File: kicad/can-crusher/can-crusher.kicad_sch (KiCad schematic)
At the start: 1 part

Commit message: Schematic Work in progress
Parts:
- added J?: Stepper Left, symbol Connector:Conn_01x04_Male
- added J?: Stepper Right, symbol Connector:Conn_01x04_Male
- added R?: 1000, symbol Device:R
- added SW?: Reboot, symbol Switch:SW_Push
- added U? (x2): BTT_TMC2209, symbol btt_tmc2209:BTT_TMC2209
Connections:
- net GND: now reaches U?.13 (GND)
- net GND: now also U?.18 (GND), U?.23 (GND), U?.28 (GND), U?.3 (GND), U?.33 (AGND), U?.38 (GND), U?.8 (GND), SW?.2, U?.15 (GND), U?.15 (GND), U?.5 (PDN), U?.5 (PDN), U?.6 (CLK), U?.6 (CLK), U?.9 (GND), U?.9 (GND)
- net at U?.14 (GPIO10): now also U?.1 (EN)
- net at U?.15 (GPIO11): now also U?.7 (STEP)
- net at U?.16 (GPIO12): now also U?.8 (DIR)
- net at U?.17 (GPIO13): now also U?.17 (DIAG)
- net at U?.19 (GPIO14): now also U?.2 (MS1)
- net at U?.20 (GPIO15): now also U?.3 (MS2)
- net at U?.21 (GPIO16): now also U?.3 (MS2)
- net at U?.22 (GPIO17): now also U?.2 (MS1)
- net at U?.24 (GPIO18): now also U?.17 (DIAG)
- net at U?.25 (GPIO19): now also U?.8 (DIR)
- net at U?.26 (GPIO20): now also U?.7 (STEP)
- net at U?.27 (GPIO21): now also U?.1 (EN)
- net at U?.30 (RUN): now also SW?.1
- net +3.3V: now reaches U?.36 (3V3)
- net +3.3V: now also U?.10 (VDD), U?.10 (VDD)
- net at U?.6 (GPIO4): now also R?.2
- net at U?.7 (GPIO5): now also R?.1, U?.4 (PDN), U?.4 (PDN)
- new net: J?.1 (Pin_1), U?.14 (A1) (x2)
- new net: J?.2 (Pin_2), U?.13 (A2) (x2)
- new net: J?.3 (Pin_3), U?.12 (B1) (x2)
- new net: J?.4 (Pin_4), U?.11 (B2) (x2)
- new net +12V: U?.16 (VM), U?.16 (VM)

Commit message: Schematic work-in-progress checkpoint
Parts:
- added J2: Control UART, symbol Connector:Conn_01x06_Female
- added J3: Ext power, symbol Connector:Conn_01x02_Male
- gave numbers to parts that had none: 7
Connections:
- net GND: now also J2.6 (Pin_6), J3.2 (Pin_2)
- net STEP_TXRX: now reaches U1.4 (PDN), U2.7 (GPIO5), U3.4 (PDN)
- net STEP_TXRX: now also R1.2; no longer R1.1
- net at U2.1 (GPIO0): now also J2.2 (Pin_2)
- net at U2.2 (GPIO1): now also J2.3 (Pin_3)
- net VCC: now reaches U2.39 (VSYS)
- net VCC: now also J3.1 (Pin_1)
- net at U2.6 (GPIO4): now also R1.1; no longer R1.2
- no-connect marks 0 -> 21
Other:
- note added: "ERC Flags"
- note added: "EXT POWER"
- note added: "External power when USB is disconnected. 1.8-5.5 volts regulated by onboard Pico buck/boost."
- note added: "For future interface so we don't need to recompile code to exercise and test motors."
- note added: "STEPPER TX/UX"
- note added: "Single wire RS483 style protocol is used to set advanced controls on TMC2209"
- note added: "UART Control Port"
- moved on the sheet: J1, J4, R1, SW1, U1, U2, U3

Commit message: Initial first pass of PCB design
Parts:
- added D1: LED_RGBK, symbol Device:LED_RGBK
- added J5: Barrel_Jack, symbol Connector:Barrel_Jack
- added J6: Expansion Port, symbol Connector:Conn_01x08_Female
- added Q1: IRF4905, Package_TO_SOT_THT:TO-220-3_Vertical, symbol Transistor_FET:IRF4905
- added R2, R3, R4: R, symbol Device:R
- added R5: 0, symbol Device:R
- added R6: 50k, symbol Device:R
- added SW2: User Interaction, symbol Switch:SW_Push
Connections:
- net +12V: now also J5.1, Q1.3 (S), R5.1, R6.2; no longer U1.16 (VM), U3.16 (VM)
- net +3.3V: now also J6.7 (Pin_7)
- net GND: now also D1.4 (K), J5.2, J6.8 (Pin_8), SW2.1
- net at U2.10 (GPIO7): now also R3.1
- net at U2.11 (GPIO8): now also R4.1
- net at U2.12 (GPIO9): now also SW2.2
- net at U2.29 (GPIO22): now also Q1.1 (G), R6.1
- net at U2.31 (GPIO26_ADC0): now also J6.3 (Pin_3)
- net at U2.32 (GPIO27_ADC1): now also J6.4 (Pin_4)
- net at U2.34 (GPIO28_ADC2): now also J6.5 (Pin_5)
- net at U2.35 (ADC_VREF): now also J6.6 (Pin_6)
- net at U2.4 (GPIO2): now also J6.1 (Pin_1)
- net at U2.5 (GPIO3): now also J6.2 (Pin_2)
- net at U2.9 (GPIO6): now also R2.1
- new net: D1.2 (GA), R3.2
- new net: D1.1 (RA), R2.2
- new net: D1.3 (BA), R4.2
- new net 12V_ON: Q1.2 (D), R5.2, U1.16 (VM), U3.16 (VM)
- no-connect marks 21 -> 10
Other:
- note added: "EXPANSION PORT"
- note added: "EXT MCU POWER"
- note added: "EXT STEPPER POWER"
- note added: "For testing give some LED color feedback and a button the user can press, so we don't always need to watch the debug logs to understand what's going on."
- note added: "LEFT Z-AXIS STEPPER CONTROL"
- note added: "Lite User Interface"
- note added: "RIGHT Z-AXIS STEPPER CONTROL"
- note added: "SOFT REBOOT SWITCH"
- note added: "Stepper motors can take anywhere between 9-24 volts. We'll just use a barrel jack and use a pre-built power supply. A P-Channel Mosfet with a Pull-Up makes us explicitly let power flow to the stepper drivers via GPIO22. Include an NC 0-ohm resistor to bypass the switch in case the design is totally wrong."
- note added: "Throw all the unused pins to a header so we can add in a few more components without having to respin the board."
- note removed: "EXT POWER"
- moved on the sheet: J1, J4, R1, SW1, U1, U3

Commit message: Added title comments, etc, to title block
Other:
- company: (none) -> https://github.com/grant-olson/can-crusher
- title: (none) -> Can Crusher Dev Board
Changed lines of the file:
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@@
 (kicad_sch (version 20211123) (generator eeschema)
   (paper "A4")
+  (title_block
+    (title "Can Crusher Dev Board")
+    (date "2022-10-10")
+    (rev "1")
+    (company "https://github.com/grant-olson/can-crusher")
+    (comment 1 "Control board for the most technilogically advanced aluminum can crusher IN THE WORLD.")
+  )
   (junction (at 207.01 46.99) (diameter 0) (color 0 0 0 0)
   )

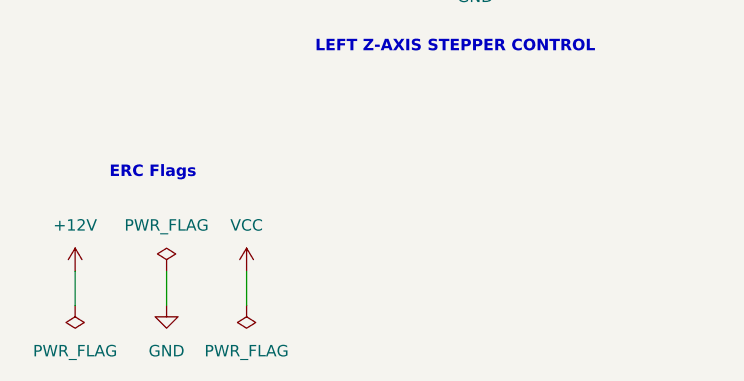
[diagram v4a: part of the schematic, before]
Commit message: Fixes for ERC checks
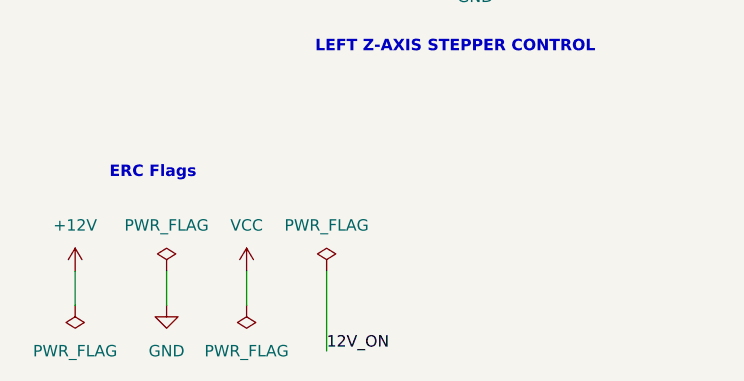
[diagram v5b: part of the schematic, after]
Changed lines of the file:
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@@
+    (stroke (width 0) (type default) (color 0 0 0 0))
+  )
+  (wire (pts (xy 49.53 184.15) (xy 49.53 193.04))
     (stroke (width 0) (type default) (color 0 0 0 0))
   )
@@
   (text "Single wire RS483 style \nprotocol is used to set \nadvanced controls on\nTMC2209\n"
     (at 88.9 26.67 0)
+    (effects (font (size 1.27 1.27)) (justify left bottom))
+  )
+  (label "12V_ON" (at 49.53 193.04 0)
     (effects (font (size 1.27 1.27)) (justify left bottom))
   )
@@
     (pin "1")
   )
-  (symbol (lib_name "BTT_TMC2209_1") (lib_id "btt_tmc2209:BTT_TMC2209") (at 237.49 118.11 0) (unit 1)
+  (symbol (lib_id "btt_tmc2209:BTT_TMC2209") (at 237.49 118.11 0) (unit 1)
     (in_bom yes) (on_board yes)
     (property "Reference" "U3" (id 0) (at 239.395 142.24 0))
@@
     (pin "1")
   )
+  (symbol (lib_id "power:PWR_FLAG") (at 49.53 184.15 0) (unit 1)
+    (in_bom yes) (on_board yes) (fields_autoplaced)
+    (property "Reference" "#FLG0102" (id 0) (at 49.53 182.245 0)
+      (effects (font (size 1.27 1.27)) hide)
+    )
+    (property "Value" "PWR_FLAG" (id 1) (at 49.53 179.07 0))
+    (property "Footprint" "" (id 2) (at 49.53 184.15 0)
+      (effects (font (size 1.27 1.27)) hide)
+    )
+    (property "Datasheet" "~" (id 3) (at 49.53 184.15 0)
+      (effects (font (size 1.27 1.27)) hide)
+    )
+    (pin "1")
+  )
   (symbol (lib_id "power:GND") (at 66.04 148.59 0) (unit 1)
     (in_bom yes) (on_board yes) (fields_autoplaced)
@@
       (reference "#FLG0101") (unit 1) (value "PWR_FLAG") (footprint "")
     )
+    (path "/8f9714ab-2f22-4d0c-918a-f2e6cc76e015"
+      (reference "#FLG0102") (unit 1) (value "PWR_FLAG") (footprint "")
+    )
     (path "/8a4f5206-01a9-48d1-8d82-8554a491299f"

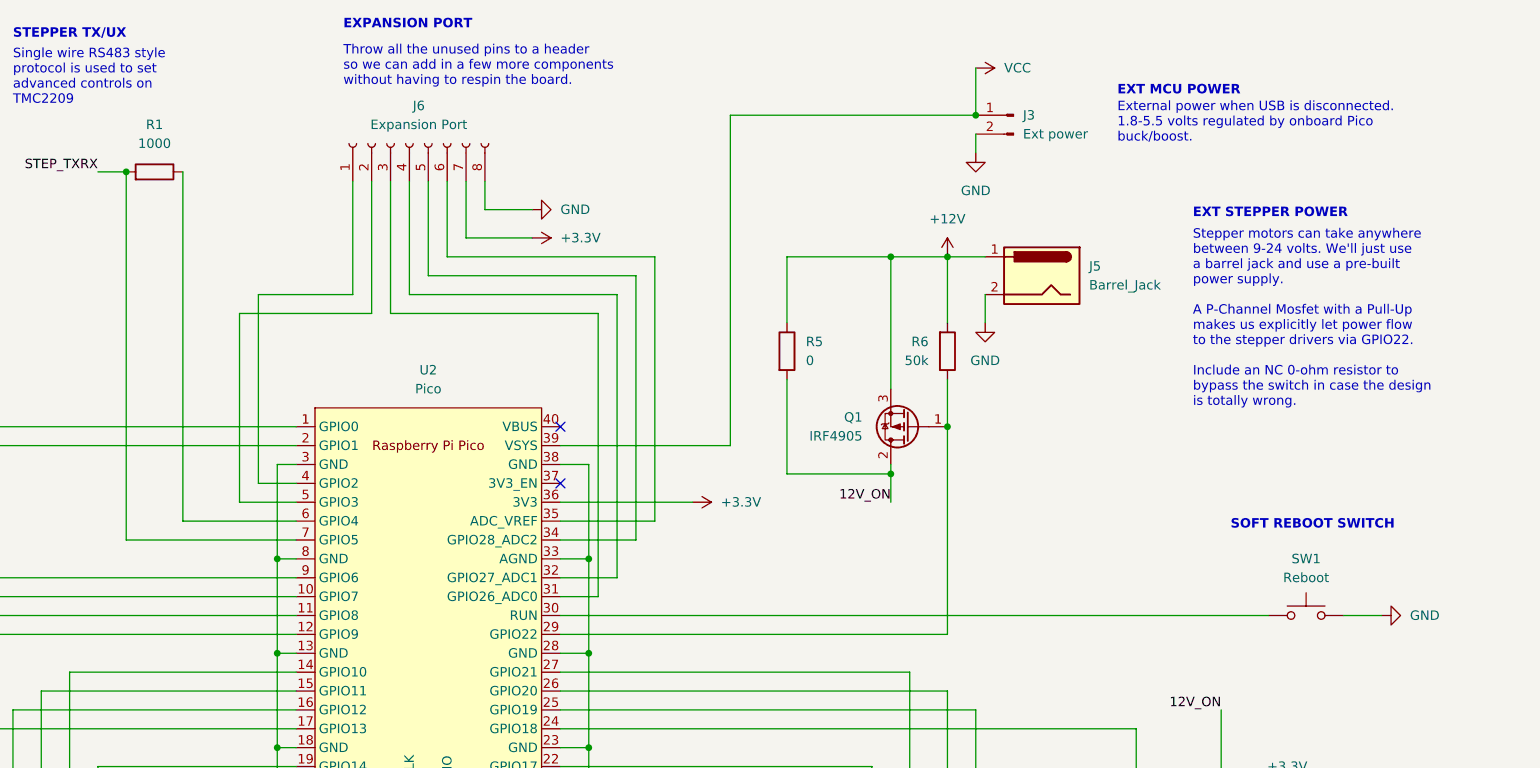
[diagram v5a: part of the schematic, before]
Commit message: More tweaks to 12 enable circuitry;First round of assigning all footprints
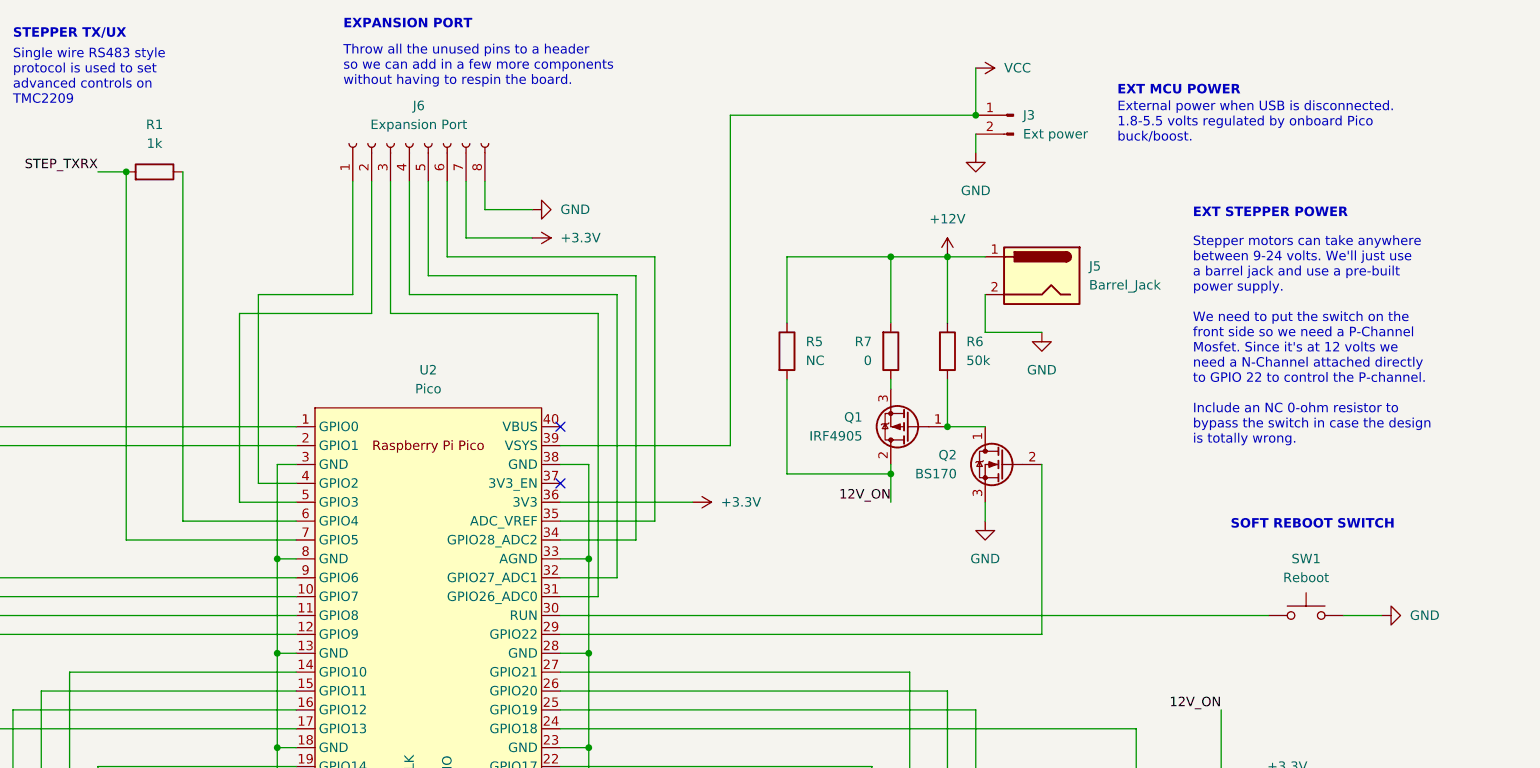
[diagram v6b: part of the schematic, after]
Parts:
- added Q2: BS170, Package_TO_SOT_THT:TO-92_Inline, symbol Transistor_FET:BS170
- added R7: 0, Resistor_THT:R_Axial_DIN0207_L6.3mm_D2.5mm_P10.16mm_Horizontal, symbol Device:R
- D1: footprint (none) -> LED_THT:LED_D5.0mm-4_RGB
- J1, J4: footprint (none) -> Connector_JST:JST_XH_B4B-XH-A_1x04_P2.50mm_Vertical
- J2: footprint (none) -> Connector_PinHeader_2.54mm:PinHeader_1x06_P2.54mm_Vertical
- J3: footprint (none) -> Connector_PinHeader_2.54mm:PinHeader_1x02_P2.54mm_Vertical
- J5: footprint (none) -> Connector_BarrelJack:BarrelJack_CUI_PJ-063AH_Horizontal
- J6: footprint (none) -> Connector_PinHeader_2.54mm:PinHeader_1x08_P2.54mm_Vertical
- R1: value 1000 -> 1k; footprint (none) -> Resistor_THT:R_Axial_DIN0207_L6.3mm_D2.5mm_P10.16mm_Horizontal
- R2, R3, R4, R6: footprint (none) -> Resistor_THT:R_Axial_DIN0207_L6.3mm_D2.5mm_P10.16mm_Horizontal
- R5: value 0 -> NC; footprint (none) -> Resistor_THT:R_Axial_DIN0207_L6.3mm_D2.5mm_P10.16mm_Horizontal
- SW1, SW2: footprint (none) -> Button_Switch_THT:SW_PUSH_6mm_H4.3mm
- U1, U3: footprint (none) -> btt_tmc2209:BTT_TMC2209
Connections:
- net +12V: now also R6.1, R7.2; no longer Q1.3 (S), R6.2
- net GND: now also Q2.3 (S)
- new net: Q1.1 (G), Q2.1 (D), R6.2
- new net: Q2.2 (G), U2.29 (GPIO22)
- new net: Q1.3 (S), R7.1
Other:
- note added: "Stepper motors can take anywhere between 9-24 volts. We'll just use a barrel jack and use a pre-built power supply. We need to put the switch on the front side so we need a P-Channel Mosfet. Since it's at 12 volts we need a N-Channel attached directly to GPIO 22 to control the P-channel. Include an NC 0-ohm resistor to bypass the switch in case the design is totally wrong."
- note removed: "Stepper motors can take anywhere between 9-24 volts. We'll just use a barrel jack and use a pre-built power supply. A P-Channel Mosfet with a Pull-Up makes us explicitly let power flow to the stepper drivers via GPIO22. Include an NC 0-ohm resistor to bypass the switch in case the design is totally wrong."
